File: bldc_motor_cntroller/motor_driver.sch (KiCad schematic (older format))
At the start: 70 parts, among them J10 MR30PW-M 15A (30A), Q3 CSD18540Q5B, Q4 CSD18540Q5B, Q5 CSD18540Q5B, Q6 CSD18540Q5B, Q7 CSD18540Q5B, Q8 CSD18540Q5B, U4 DRV8301DCAR

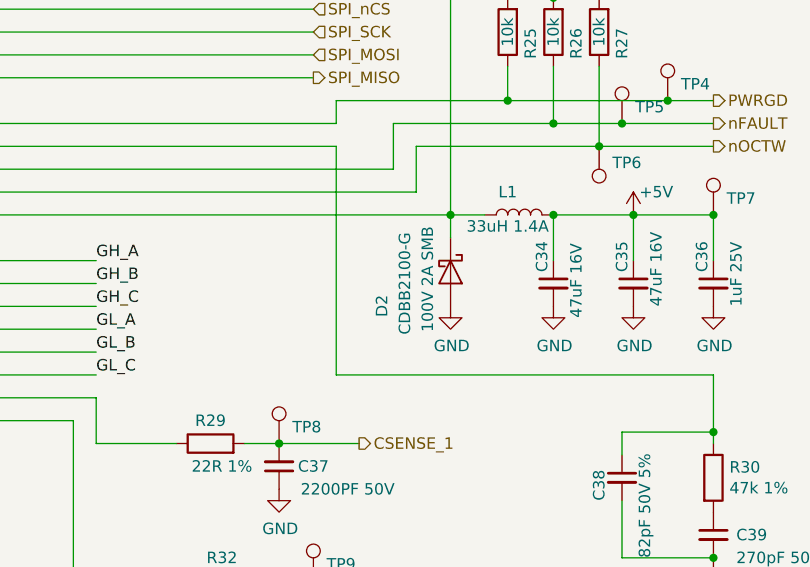
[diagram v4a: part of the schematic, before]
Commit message: combined 2.54p connectors. changed diode footprint.
Signed-off-by: azmat bilal <azmat.bilal@outlook.com>
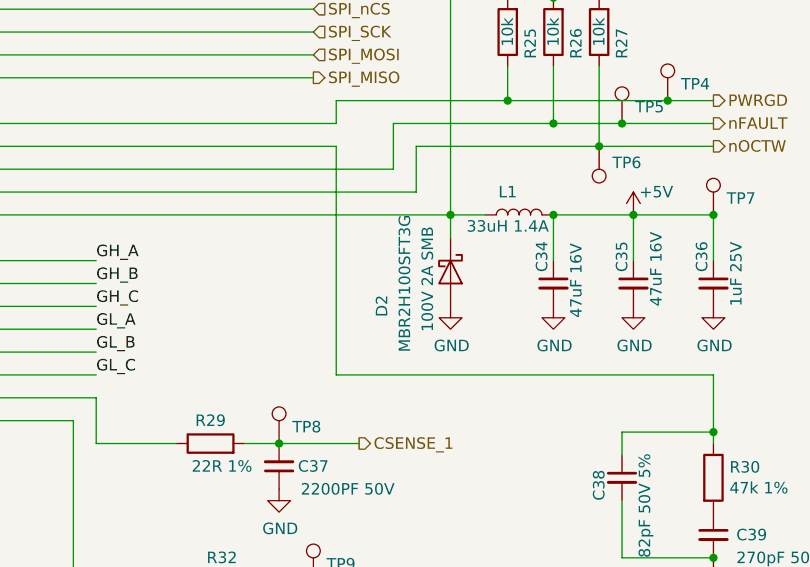
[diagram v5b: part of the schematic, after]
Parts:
- D2: footprint Diode_SMD:D_SMB -> Diode_SMD:D_SOD-123F; MPN CDBB2100-G -> MBR2H100SFT3G
- L1: footprint Inductor_SMD:L_Bourns_SRN6045TA -> Inductor_SMD:L_Taiyo-Yuden_NR-60xx; MPN (none) -> NR6045T330M
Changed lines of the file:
@@
 F 0 "L1" V 7750 3400 50  0000 C CNN
 F 1 "33uH 1.4A" V 7600 3400 50  0000 C CNN
-F 2 "Inductor_SMD:L_Bourns_SRN6045TA" H 7650 3350 50  0001 C CNN
+F 2 "Inductor_SMD:L_Taiyo-Yuden_NR-60xx" H 7650 3350 50  0001 C CNN
 F 3 "https://www.bourns.com/docs/Product-Datasheets/SRN6045.pdf" H 7650 3350 50  0001 C CNN
+F 4 "NR6045T330M" V 7650 3350 50  0001 C CNN "MPN"
 	1    7650 3350
 	0    -1   -1   0
@@
 F 0 "D2" H 7450 3300 50  0000 L CNN
 F 1 "100V 2A SMB" H 7150 3500 50  0000 L CNN
-F 2 "Diode_SMD:D_SMB" H 7350 3600 50  0001 C CNN
-F 3 "https://www.mouser.de/datasheet/2/80/CDBB240-HF_Thru503873._CDBB2100-HF_RevD-1480886.pdf" H 7350 3600 50  0001 C CNN
-F 4 "CDBB2100-G" H 7400 3400 50  0000 C CNN "MPN"
+F 2 "Diode_SMD:D_SOD-123F" H 7350 3600 50  0001 C CNN
+F 3 "" H 7350 3600 50  0001 C CNN
+F 4 "MBR2H100SFT3G" H 7400 3400 50  0000 C CNN "MPN"
 	1    7350 3600
 	0    1    1    0

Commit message: fixed a typo
Signed-off-by: azmat bilal <azmat.bilal@outlook.com>
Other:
- note added: "MP30 can handle 30A peak and 15A cont.\nif more current is needed, the connector \ncan be changed."
- note removed: "MP30 can handle 30A peak and 15A cont.\nif more current is needed, the connector \ncant be changed."
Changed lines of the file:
@@
 $EndComp
 Text Notes 7350 6450 0    50   ~ 0
-MP30 can handle 30A peak and 15A cont.\nif more current is needed, the connector \ncant be changed.
+MP30 can handle 30A peak and 15A cont.\nif more current is needed, the connector \ncan be changed.
 $EndSCHEMATC

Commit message: changed the motor conn. for thicker wires.
Signed-off-by: azmat bilal <azmat.bilal@outlook.com>
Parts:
- J10: footprint Connector_AMASS:AMASS_MR30PW-M_1x03_P3.50mm_Horizontal -> Connector_Wire:SolderWirePad_1x03_P7.62mm_Drill2.5mm
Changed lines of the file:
@@
 F 0 "J10" H 7330 6142 50  0000 L CNN
 F 1 "MR30PW-M 15A (30A)" H 7330 6051 50  0000 L CNN
-F 2 "Connector_AMASS:AMASS_MR30PW-M_1x03_P3.50mm_Horizontal" H 7250 6100 50  0001 C CNN
+F 2 "Connector_Wire:SolderWirePad_1x03_P7.62mm_Drill2.5mm" H 7250 6100 50  0001 C CNN
 F 3 "~" H 7250 6100 50  0001 C CNN
 	1    7250 6100

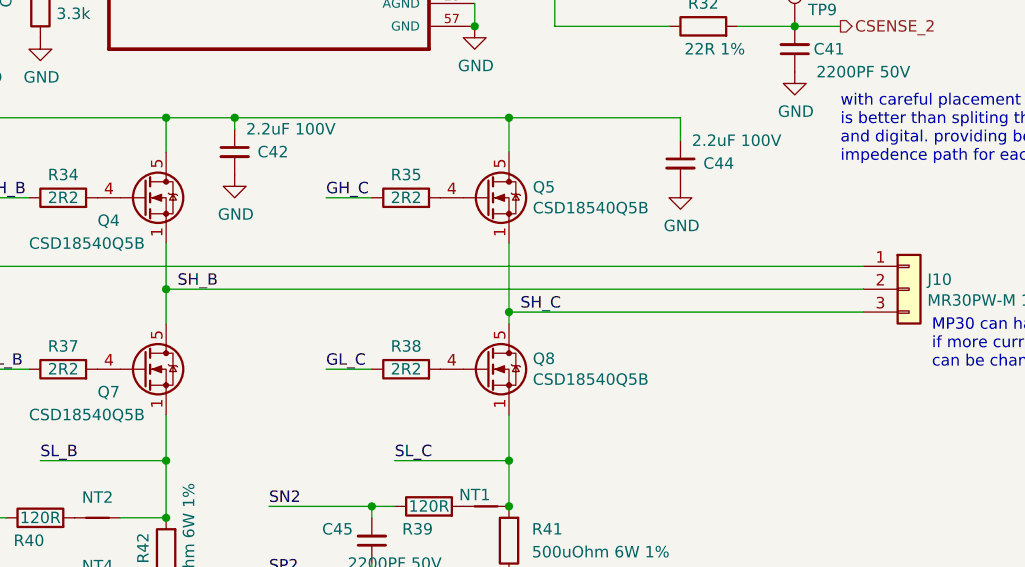
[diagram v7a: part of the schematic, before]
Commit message: increase layer count to 4. routinng cont. swapped motor outputs.
Signed-off-by: azmat bilal <azmat.bilal@outlook.com>
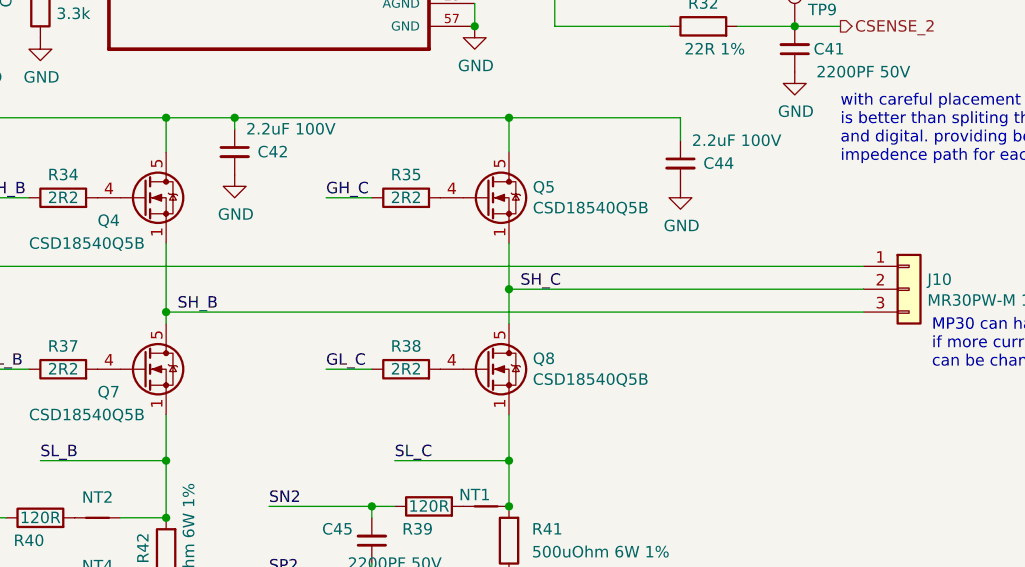
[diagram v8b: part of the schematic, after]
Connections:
- net SH_B: now also J10.3 (Pin_3); no longer J10.2 (Pin_2)
- net SH_C: now also J10.2 (Pin_2); no longer J10.3 (Pin_3)
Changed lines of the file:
@@
 Wire Wire Line
 	2500 5900 2500 6000
-Wire Wire Line
-	5500 5900 5500 6200
-Wire Wire Line
-	4000 5900 4000 6100
 $Comp
 L Device:Net-Tie_2 NT2
@@
 Text Label 2550 6000 0    50   ~ 0
 SH_A
-Text Label 4050 6100 0    50   ~ 0
+Text Label 4050 6200 0    50   ~ 0
 SH_B
-Text Label 5550 6200 0    50   ~ 0
+Text Label 5550 6100 0    50   ~ 0
 SH_C
 Wire Wire Line
@@
 Wire Wire Line
 	2500 6000 2500 6250
-Wire Wire Line
-	4000 6100 7050 6100
-Connection ~ 4000 6100
-Wire Wire Line
-	4000 6100 4000 6250
-Wire Wire Line
-	5500 6200 7050 6200
-Connection ~ 5500 6200
-Wire Wire Line
-	5500 6200 5500 6250
 Text Label 2100 6850 0    50   ~ 0
 SL_A
@@
 Text Notes 7350 6450 0    50   ~ 0
 MP30 can handle 30A peak and 15A cont.\nif more current is needed, the connector \ncan be changed.
+Wire Wire Line
+	4000 5900 4000 6200
+Wire Wire Line
+	5500 5900 5500 6100
+Wire Wire Line
+	5500 6100 7050 6100
+Connection ~ 5500 6100
+Wire Wire Line
+	5500 6100 5500 6250
+Wire Wire Line
+	7050 6200 4000 6200
+Connection ~ 4000 6200
+Wire Wire Line
+	4000 6200 4000 6250
 $EndSCHEMATC
